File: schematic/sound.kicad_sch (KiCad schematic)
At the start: 12 parts

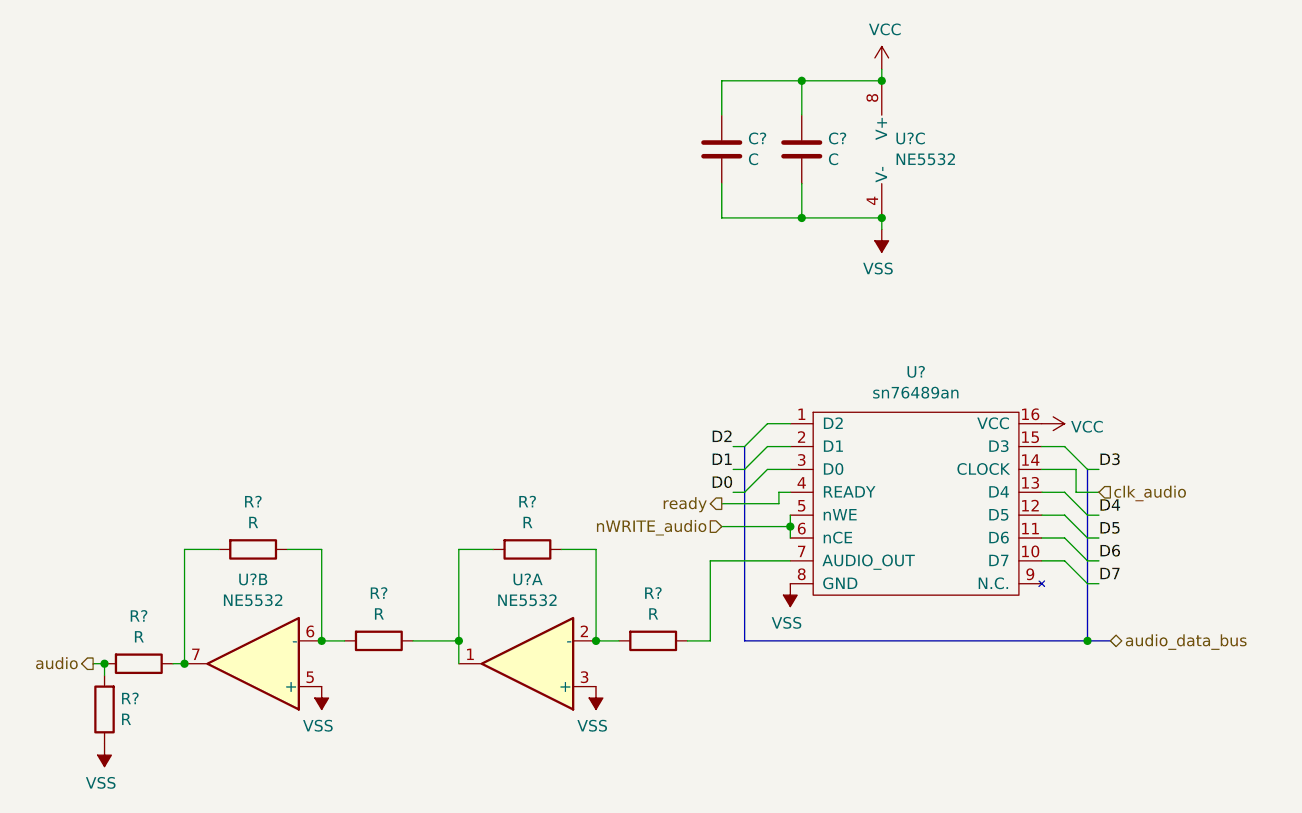
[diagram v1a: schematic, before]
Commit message: revised schematic into sheets for easier design. Looks much better.
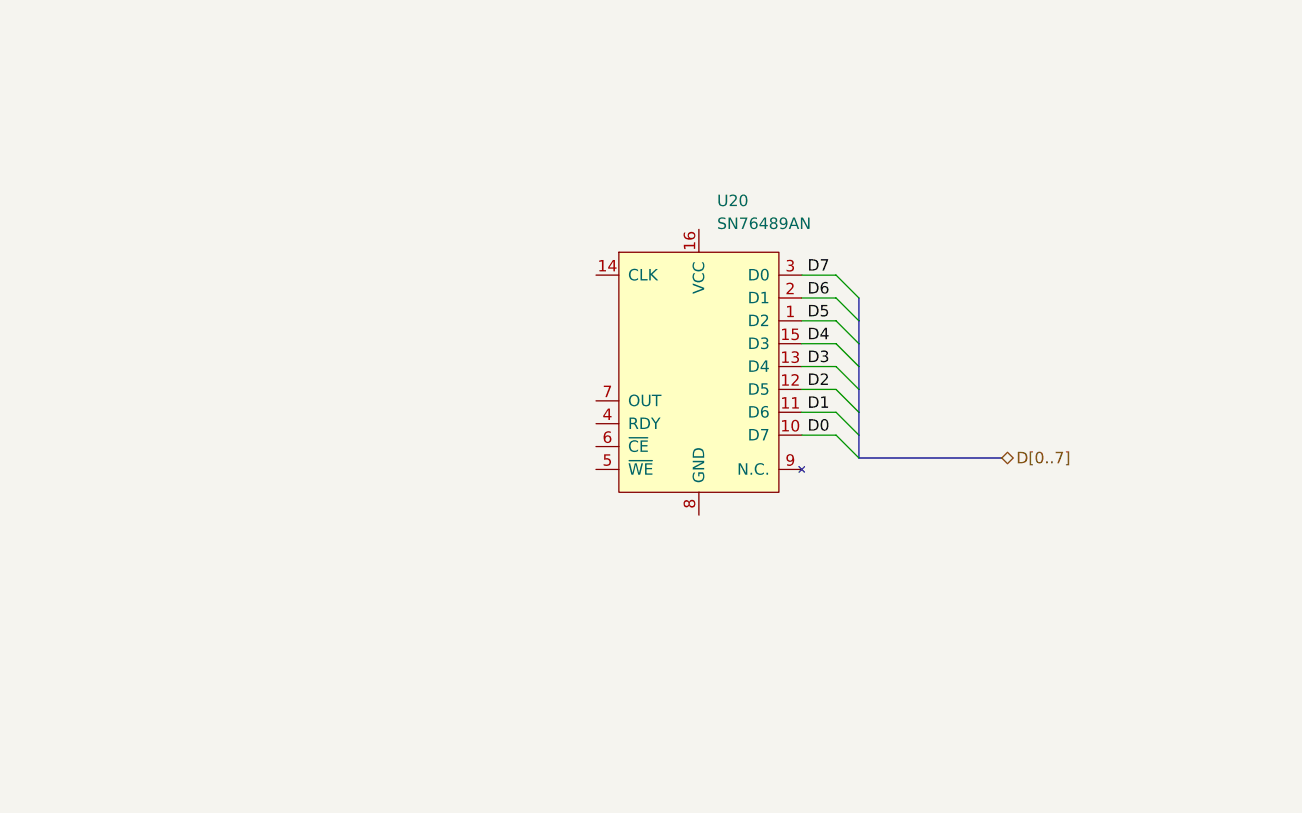
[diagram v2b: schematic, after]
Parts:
- removed C? (x2): C, symbol Device:C
- removed R? (x6): R, symbol Device:R
- removed U?: sn76489an, symbol Vintage_PC_Audio:sn76489an
- removed U? (x3): NE5532, symbol Amplifier_Operational:NE5532
- added U20: SN76489AN, symbol Vintage_PC_Audio:SN76489AN
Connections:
- net D0: now also U20.10 (D7)
- net D1: now also U20.11 (D6)
- net D2: now also U20.12 (D5)
- net D3: now also U20.13 (D4)
- net D4: now also U20.15 (D3)
- net D5: now also U20.1 (D2)
- net D6: now also U20.2 (D1)
- net D7: now also U20.3 (D0)

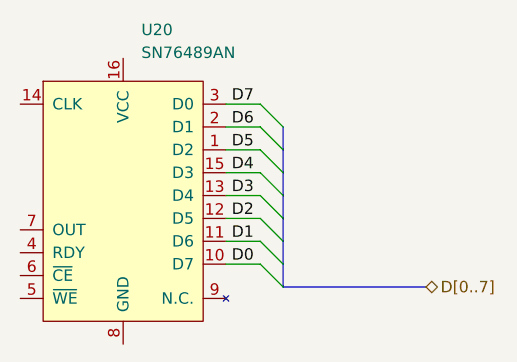
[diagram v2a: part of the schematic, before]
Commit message: changed all vintage library names to better represent future ideas. Removed parts not needed... for now. Updated schmematic symbols.
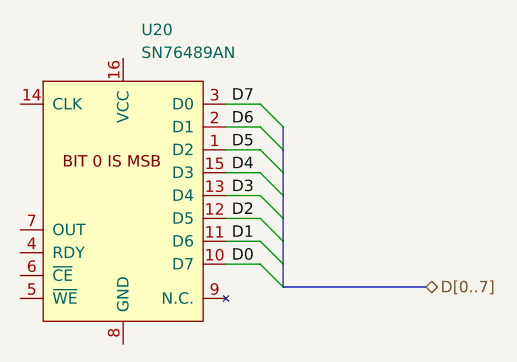
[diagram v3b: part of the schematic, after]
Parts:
- U20: symbol Vintage_PC_Audio:SN76489AN -> Vintage_Audio_Synth:SN76489AN
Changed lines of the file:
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@@
     (effects (font (size 1.27 1.27)) (justify left))
   )
-  (symbol (lib_id "Vintage_PC_Audio:SN76489AN") (at 149.86 69.85 0) (unit 1)
+  (symbol (lib_id "Vintage_Audio_Synth:SN76489AN") (at 149.86 69.85 0) (unit 1)
     (in_bom yes) (on_board yes) (fields_autoplaced)
     (property "Reference" "U20" (id 0) (at 151.8794 60.325 0)

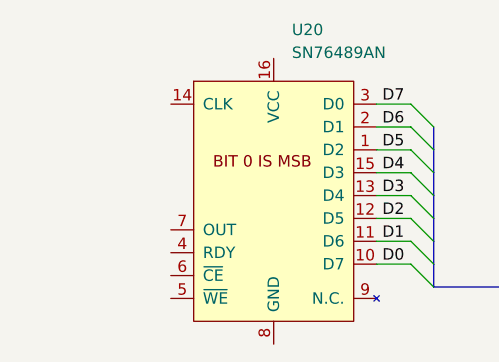
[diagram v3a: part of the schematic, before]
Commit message: Up to pin 29 on z80 done. Address 0 to 10 left. Only tracing to its end point for the most part. Each chip gets traced chip to chip in this manned
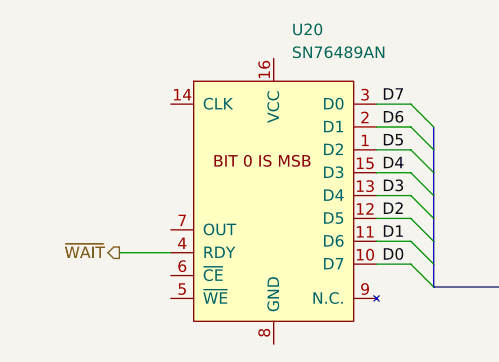
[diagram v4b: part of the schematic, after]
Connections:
- net ~{WAIT}: now reaches U20.4 (RDY)
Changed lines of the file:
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@@
+    (stroke (width 0) (type default) (color 0 0 0 0))
+  )
+  (wire (pts (xy 132.715 85.09) (xy 138.43 85.09))
     (stroke (width 0) (type default) (color 0 0 0 0))
   )
@@
     (effects (font (size 1.27 1.27)) (justify left))
   )
+  (hierarchical_label "~{WAIT}" (shape output) (at 132.715 85.09 180)
+    (effects (font (size 1.27 1.27)) (justify right))
+  )
   (symbol (lib_id "Vintage_Audio_Synth:SN76489AN") (at 149.86 69.85 0) (unit 1)

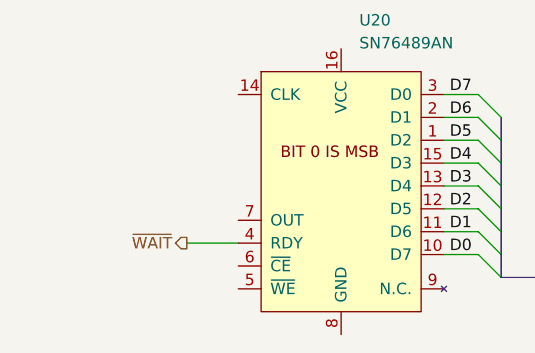
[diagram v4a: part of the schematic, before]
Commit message: added u6 decoder lines, renamed a few lines to make sense to there destination.
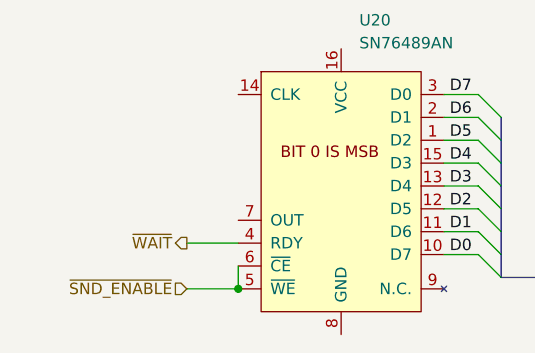
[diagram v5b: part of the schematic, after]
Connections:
- net ~{SND_ENABLE}: now reaches U20.5 (~{WE})
- net ~{SND_ENABLE}: now also U20.6 (~{CE})
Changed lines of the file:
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@@
 (kicad_sch (version 20211123) (generator eeschema)
   (paper "A4")
+  (junction (at 138.43 90.17) (diameter 0) (color 0 0 0 0)
+  )
   (bus_entry (at 165.1 78.74) (size 2.54 2.54)
     (stroke (width 0) (type default) (color 0 0 0 0))
@@
     (stroke (width 0) (type default) (color 0 0 0 0))
   )
+  (wire (pts (xy 138.43 87.63) (xy 138.43 90.17))
+    (stroke (width 0) (type default) (color 0 0 0 0))
+  )
   (bus (pts (xy 167.64 88.9) (xy 183.515 88.9))
     (stroke (width 0) (type default) (color 0 0 0 0))
@@
   )
   (wire (pts (xy 161.29 71.12) (xy 165.1 71.12))
+    (stroke (width 0) (type default) (color 0 0 0 0))
+  )
+  (wire (pts (xy 132.715 90.17) (xy 138.43 90.17))
     (stroke (width 0) (type default) (color 0 0 0 0))
   )
@@
     (effects (font (size 1.27 1.27)) (justify left))
   )
+  (hierarchical_label "~{SND_ENABLE}" (shape input) (at 132.715 90.17 180)
+    (effects (font (size 1.27 1.27)) (justify right))
+  )
   (hierarchical_label "~{WAIT}" (shape output) (at 132.715 85.09 180)

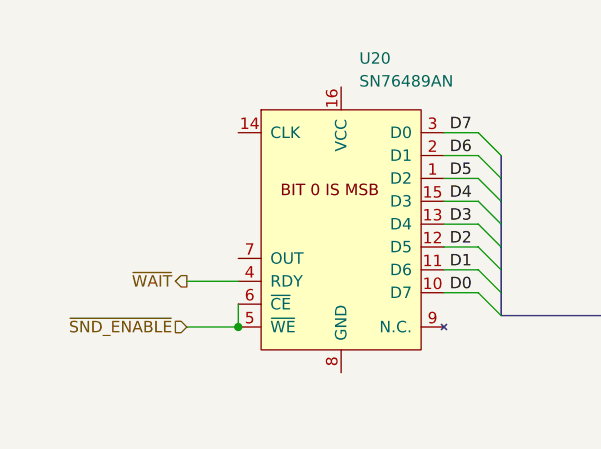
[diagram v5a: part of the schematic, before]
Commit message: completed sound block, finished cart io port, and finished decoder.
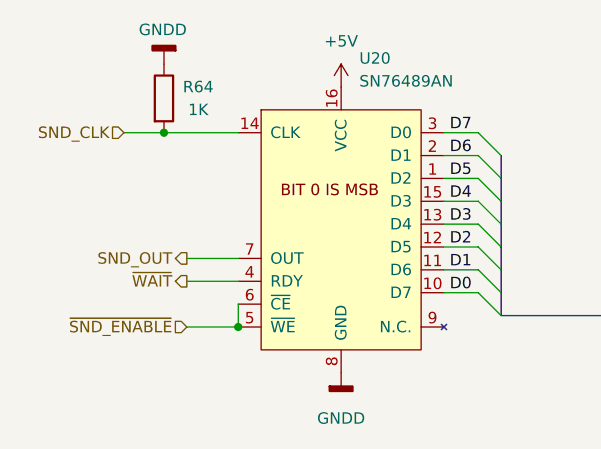
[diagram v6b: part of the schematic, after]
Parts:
- added R64: 1K, symbol Device:R
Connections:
- net SND_CLK: now reaches U20.14 (CLK)
- net SND_CLK: now also R64.2
- net +5V: now reaches U20.16 (VCC)
- net SND_OUT: now reaches U20.7 (OUT)
- net GNDD: now reaches U20.8 (GND)
- net GNDD: now also R64.1
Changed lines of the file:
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@@
 (kicad_sch (version 20211123) (generator eeschema)
   (paper "A4")
+  (junction (at 130.175 68.58) (diameter 0) (color 0 0 0 0)
+  )
   (junction (at 138.43 90.17) (diameter 0) (color 0 0 0 0)
   )
@@
     (stroke (width 0) (type default) (color 0 0 0 0))
   )
+  (wire (pts (xy 130.175 68.58) (xy 138.43 68.58))
+    (stroke (width 0) (type default) (color 0 0 0 0))
+  )
+  (wire (pts (xy 125.73 68.58) (xy 130.175 68.58))
+    (stroke (width 0) (type default) (color 0 0 0 0))
+  )
   (bus (pts (xy 167.64 81.28) (xy 167.64 83.82))
     (stroke (width 0) (type default) (color 0 0 0 0))
@@
   )
   (wire (pts (xy 161.29 68.58) (xy 165.1 68.58))
+    (stroke (width 0) (type default) (color 0 0 0 0))
+  )
+  (wire (pts (xy 132.715 82.55) (xy 138.43 82.55))
     (stroke (width 0) (type default) (color 0 0 0 0))
   )
@@
     (effects (font (size 1.27 1.27)) (justify right))
   )
+  (hierarchical_label "SND_OUT" (shape output) (at 132.715 82.55 180)
+    (effects (font (size 1.27 1.27)) (justify right))
+  )
+  (hierarchical_label "SND_CLK" (shape input) (at 125.73 68.58 180)
+    (effects (font (size 1.27 1.27)) (justify right))
+  )
   (hierarchical_label "~{WAIT}" (shape output) (at 132.715 85.09 180)
     (effects (font (size 1.27 1.27)) (justify right))
+  )
+  (symbol (lib_id "power:GNDD") (at 149.86 95.25 0) (unit 1)
+    (in_bom yes) (on_board yes) (fields_autoplaced)
+    (property "Reference" "#PWR?" (id 0) (at 149.86 101.6 0)
+      (effects (font (size 1.27 1.27)) hide)
+    )
+    (property "Value" "GNDD" (id 1) (at 149.86 100.33 0))
+    (property "Footprint" "" (id 2) (at 149.86 95.25 0)
+      (effects (font (size 1.27 1.27)) hide)
+    )
+    (property "Datasheet" "" (id 3) (at 149.86 95.25 0)
+      (effects (font (size 1.27 1.27)) hide)
+    )
+    (pin "1")
+  )
+  (symbol (lib_id "power:+5V") (at 149.86 63.5 0) (unit 1)
+    (in_bom yes) (on_board yes) (fields_autoplaced)
+    (property "Reference" "#PWR?" (id 0) (at 149.86 67.31 0)
+      (effects (font (size 1.27 1.27)) hide)
+    )
+    (property "Value" "+5V" (id 1) (at 149.86 58.42 0))
+    (property "Footprint" "" (id 2) (at 149.86 63.5 0)
+      (effects (font (size 1.27 1.27)) hide)
+    )
+    (property "Datasheet" "" (id 3) (at 149.86 63.5 0)
+      (effects (font (size 1.27 1.27)) hide)
+    )
+    (pin "1")
   )
   (symbol (lib_id "Vintage_Audio_Synth:SN76489AN") (at 149.86 69.85 0) (unit 1)
@@
     (pin "9")
   )
+  (symbol (lib_id "power:GNDD") (at 130.175 60.96 180) (unit 1)
+    (in_bom yes) (on_board yes)
+    (property "Reference" "#PWR?" (id 0) (at 130.175 54.61 0)
+      (effects (font (size 1.27 1.27)) hide)
+    )
+    (property "Value" "GNDD" (id 1) (at 132.715 57.15 0)
+      (effects (font (size 1.27 1.27)) (justify left))
+    )
+    (property "Footprint" "" (id 2) (at 130.175 60.96 0)
+      (effects (font (size 1.27 1.27)) hide)
+    )
+    (property "Datasheet" "" (id 3) (at 130.175 60.96 0)
+      (effects (font (size 1.27 1.27)) hide)
+    )
+    (pin "1")
+  )
+  (symbol (lib_id "Device:R") (at 130.175 64.77 0) (unit 1)
+    (in_bom yes) (on_board yes)
+    (property "Reference" "R64" (id 0) (at 133.985 63.5 0))
+    (property "Value" "1K" (id 1) (at 133.985 66.04 0))
+    (property "Footprint" "" (id 2) (at 128.397 64.77 90)
+      (effects (font (size 1.27 1.27)) hide)
+    )
+    (property "Datasheet" "~" (id 3) (at 130.175 64.77 0)
+      (effects (font (size 1.27 1.27)) hide)
+    )
+    (pin "1")
+    (pin "2")
+  )
 )

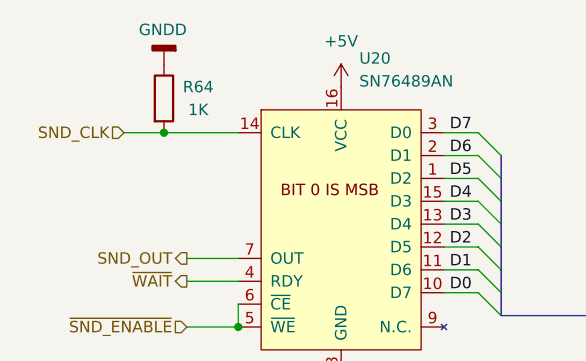
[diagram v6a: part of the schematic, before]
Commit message: Cleanup clock-reset-invert schematic. Checked against wiki.console5.com/wiki/Colecovision. Had a inverter backwards (after cleanup it was obvious since its a standard circuit). Everything else checks, though schematic is missing the wire connection on D8B from 8 to 12. Verified that mine is correct and the wiki is incorrect.
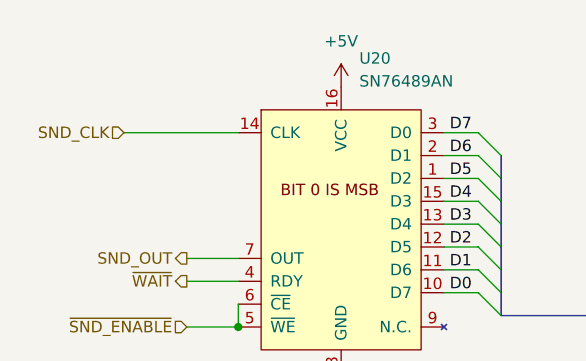
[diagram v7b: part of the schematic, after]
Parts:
- removed R64: 1K, symbol Device:R
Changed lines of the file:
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@@
 (kicad_sch (version 20211123) (generator eeschema)
   (paper "A4")
-  (junction (at 130.175 68.58) (diameter 0) (color 0 0 0 0)
-  )
   (junction (at 138.43 90.17) (diameter 0) (color 0 0 0 0)
   )
@@
     (stroke (width 0) (type default) (color 0 0 0 0))
   )
-  (wire (pts (xy 130.175 68.58) (xy 138.43 68.58))
-    (stroke (width 0) (type default) (color 0 0 0 0))
-  )
-  (wire (pts (xy 125.73 68.58) (xy 130.175 68.58))
+  (wire (pts (xy 125.73 68.58) (xy 138.43 68.58))
     (stroke (width 0) (type default) (color 0 0 0 0))
   )
@@
     (pin "9")
   )
-  (symbol (lib_id "power:GNDD") (at 130.175 60.96 180) (unit 1)
-    (in_bom yes) (on_board yes)
-    (property "Reference" "#PWR?" (id 0) (at 130.175 54.61 0)
-      (effects (font (size 1.27 1.27)) hide)
-    )
-    (property "Value" "GNDD" (id 1) (at 132.715 57.15 0)
-      (effects (font (size 1.27 1.27)) (justify left))
-    )
-    (property "Footprint" "" (id 2) (at 130.175 60.96 0)
-      (effects (font (size 1.27 1.27)) hide)
-    )
-    (property "Datasheet" "" (id 3) (at 130.175 60.96 0)
-      (effects (font (size 1.27 1.27)) hide)
-    )
-    (pin "1")
-  )
-  (symbol (lib_id "Device:R") (at 130.175 64.77 0) (unit 1)
-    (in_bom yes) (on_board yes)
-    (property "Reference" "R64" (id 0) (at 133.985 63.5 0))
-    (property "Value" "1K" (id 1) (at 133.985 66.04 0))
-    (property "Footprint" "" (id 2) (at 128.397 64.77 90)
-      (effects (font (size 1.27 1.27)) hide)
-    )
-    (property "Datasheet" "~" (id 3) (at 130.175 64.77 0)
-      (effects (font (size 1.27 1.27)) hide)
-    )
-    (pin "1")
-    (pin "2")
-  )
 )

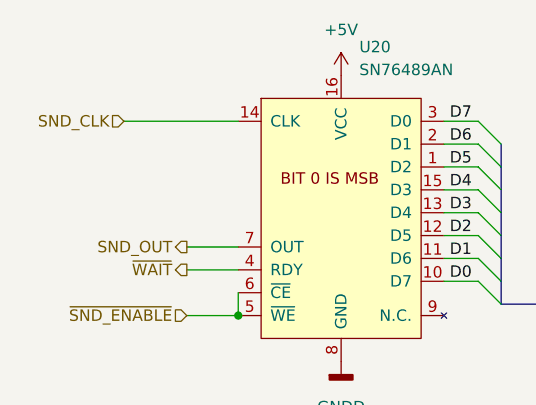
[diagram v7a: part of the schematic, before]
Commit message: cleanup on the controller schematic. Checked against wiki.console5.com/wiki/Colecovision. Found a mistake with INT line thanks to the wiki. R21/R22 is reversed between the schematics. Aka R21 is placed on the output of 3. Which actually makes sense, but isn't the way its done on my REV F. R25/R23 match the wiki and that has R25 the pull down on the output pin 6 of the nand. Looks like R21 is a board mistake, but I'll keep it in since its correct for documentation purposes.
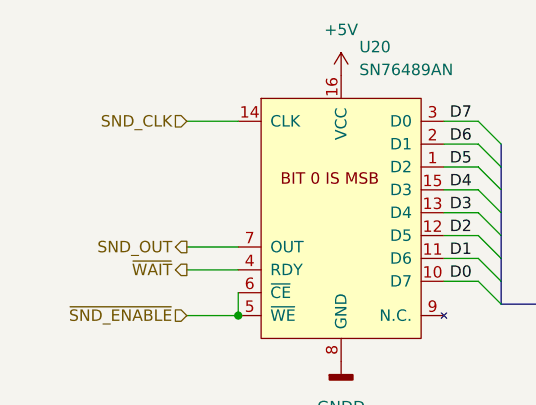
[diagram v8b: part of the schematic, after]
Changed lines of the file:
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@@
     (stroke (width 0) (type default) (color 0 0 0 0))
   )
-  (wire (pts (xy 125.73 68.58) (xy 138.43 68.58))
+  (wire (pts (xy 132.715 68.58) (xy 138.43 68.58))
     (stroke (width 0) (type default) (color 0 0 0 0))
   )
@@
     (effects (font (size 1.27 1.27)) (justify right))
   )
-  (hierarchical_label "SND_CLK" (shape input) (at 125.73 68.58 180)
+  (hierarchical_label "SND_CLK" (shape input) (at 132.715 68.58 180)
     (effects (font (size 1.27 1.27)) (justify right))
   )
